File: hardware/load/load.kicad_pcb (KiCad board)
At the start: 2 copper layers, 116 parts, among them J101 vin_kelvin, J102 uart, J103 panel, J105 vin, J106 dut, J107 fan, J108 fuse 20A, J401 temp_sensor, Q302 2sb1357, Q501 2STC4468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

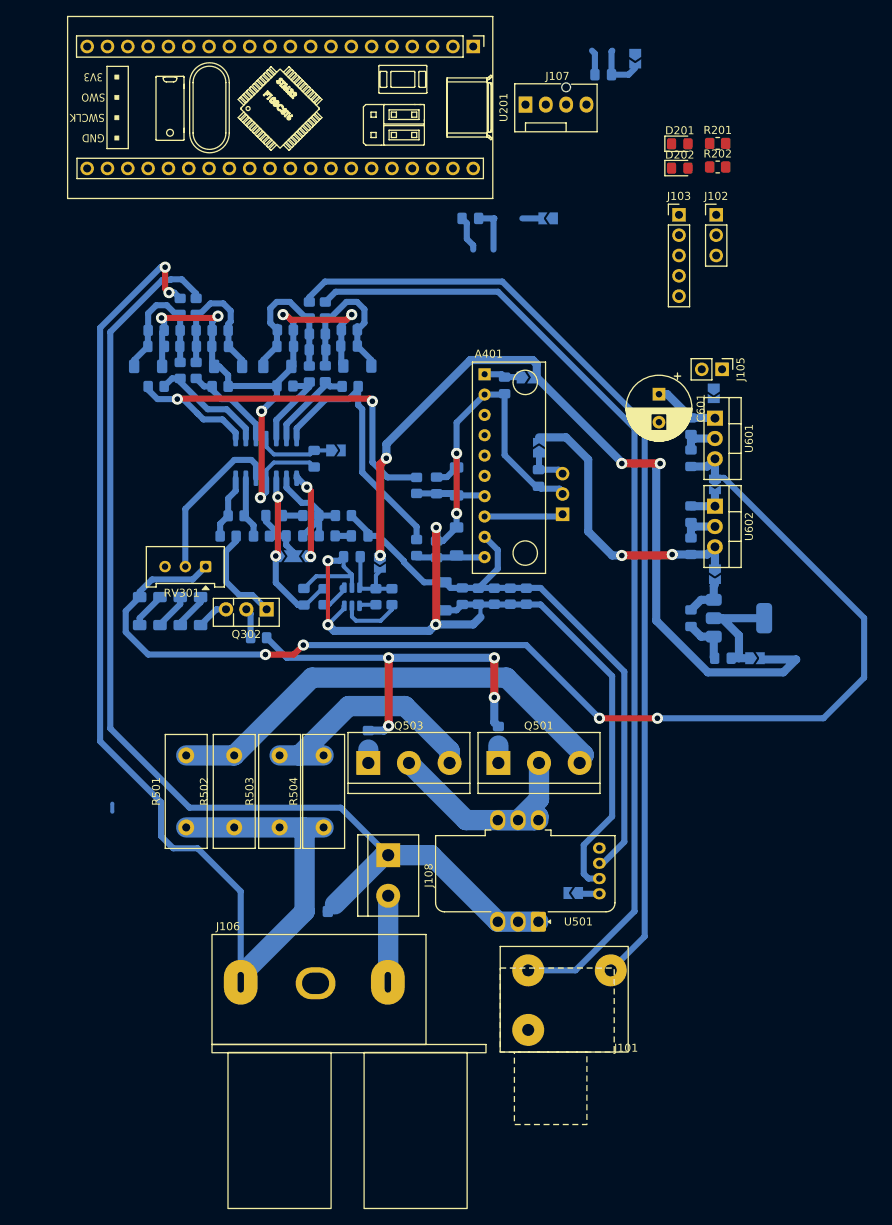
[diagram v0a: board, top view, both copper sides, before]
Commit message: feat(load): route logic and optmize layout
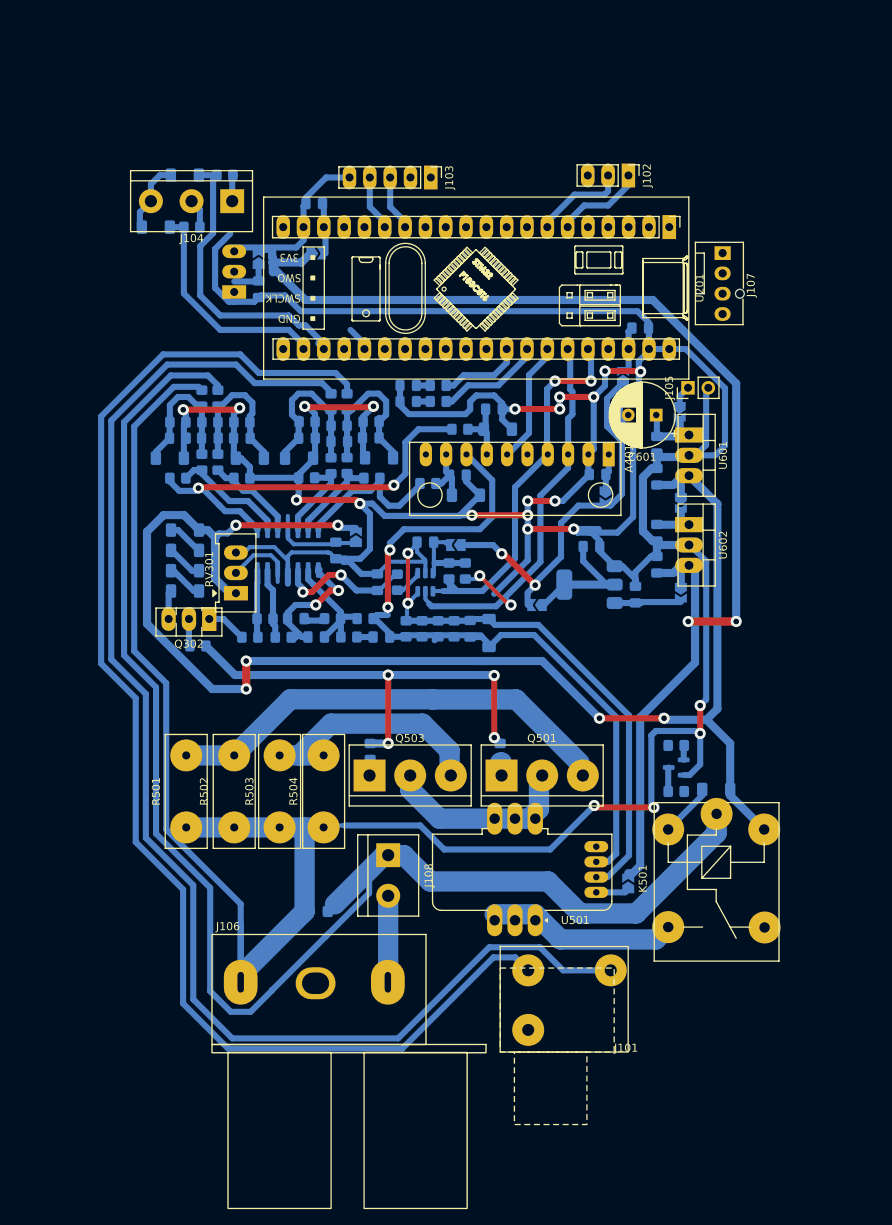
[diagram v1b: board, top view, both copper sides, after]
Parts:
- removed JP301: enable_analog_feedback, Jumper:SolderJumper-3_P2.0mm_Open_TrianglePad1.0x1.5mm
- added D203: 3.3 < V < 5.1, Diode_SMD:D_MiniMELF, B.Cu at (165.0, 56.0)
- added D204: 3.3 < V < 5.1, Diode_SMD:D_MiniMELF, B.Cu at (168.6, 49.5)
- added D501: LL4148, Diode_SMD:D_MiniMELF, B.Cu at (235.0, 126.2)
- added J104: external_trigger, TerminalBlock:TerminalBlock_bornier-3_P5.08mm, F.Cu at (174.5, 52.7)
- added K501: SANYOU_SRD_Form_C, Relay_THT:Relay_SPDT_SANYOU_SRD_Series_Form_C, F.Cu at (235.1, 129.3)
- added Q502: BC817, Package_TO_SOT_SMD:SOT-23, B.Cu at (230.0, 123.5)
- added R203: 2.2k, Resistor_SMD:R_0805_2012Metric_Pad1.20x1.40mm_HandSolder, B.Cu at (173.6, 49.5)
- added R204: 2.2k, Resistor_SMD:R_0805_2012Metric_Pad1.20x1.40mm_HandSolder, B.Cu at (169.5, 56.0)
- added R505: 150R, Resistor_SMD:R_0805_2012Metric_Pad1.20x1.40mm_HandSolder, B.Cu at (230.0, 126.5)
- added R506: 1k, Resistor_SMD:R_0805_2012Metric_Pad1.20x1.40mm_HandSolder, B.Cu at (230.0, 120.8)
- D201, D202, R201, R202: moved to B.Cu
- moved J401 49.6 mm to (174.8, 64.1)
- moved R201 46.2 mm to (200.2, 75.8), turned to 180 degrees
- moved R202 45.6 mm to (200.2, 77.8), turned to 180 degrees
- moved D201 45.4 mm to (196.5, 75.8)
- moved D202 44.8 mm to (196.5, 77.8)
- moved JP404 42.2 mm to (177.8, 60.0)
- moved C414 42.2 mm to (177.8, 63.7)
- moved JP202 39.8 mm to (223.4, 74.7), turned to 90 degrees
- moved U201 33.3 mm to (229.1, 56.0)
- moved C202 32.0 mm to (225.5, 68.6), turned to 0 degrees
- moved J103 31.4 mm to (199.3, 49.8), turned to -90 degrees
- moved J107 30.8 mm to (235.8, 59.2), turned to -90 degrees
- moved JP201 29.3 mm to (185.0, 59.2), turned to 0 degrees
- moved NT501 28.3 mm to (187.8, 130.8), turned to 0 degrees
- moved JP604 28.0 mm to (212.6, 103.2), turned to 180 degrees
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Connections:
- C302 pad 2: Net-(JP301-C) -> Net-(C302-Pad2)
- C303 pad 2: Net-(JP301-C) -> Net-(C302-Pad2)
- R201 pad 1: Net-(U201-PB0) -> Net-(U201-PA7)
- R202 pad 1: Net-(U201-PB1) -> Net-(U201-PB0)
- R304 pad 1: Net-(JP301-C) -> Net-(C302-Pad2)
- U201 pad 13: /analog/alert -> unconnected-(U201-PB5-Pad13)
- U201 pad 22: unconnected-(U201-PC13-Pad22) -> Net-(D203-K)
- U201 pad 23: unconnected-(U201-PC14-Pad23) -> Net-(D204-K)
- U201 pad 31: /stm32/fan -> unconnected-(U201-PA6-Pad31)
- U201 pad 32: unconnected-(U201-PA7-Pad32) -> Net-(U201-PA7)
- U201 pad 34: Net-(U201-PB1) -> /analog/alert
- U201 pad 5: unconnected-(U201-PA8-Pad5) -> /stm32/fan
- U301 pad 8: Net-(JP301-A) -> Net-(C302-Pad2)
- U501 pad 1: /analog/vin+ -> Net-(U501-IN1)
- U501 pad 2: /analog/vin+ -> Net-(U501-IN1)
- U501 pad 3: /analog/vin+ -> Net-(U501-IN1)
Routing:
- net GND: track 210.5 -> 532.5 mm, vias 12 -> 24
- net +5V: track 36.5 -> 157.7 mm
- net +3V3: track 104.2 -> 47.9 mm, vias 4 -> 2
- net /analog/vin_kelvin+: track 120.8 -> 169.7 mm
- net /analog/scl: track 7.74 -> 55.6 mm, vias 0 -> 2
- net /analog/sda: track 1.99 -> 49.3 mm, vias 0 -> 2
- net /analog/vin+: track 138.3 -> 185.2 mm
- net /analog/vin_kelvin-: track 123.0 -> 165.2 mm
- net Net-(D204-K): track 0.00 -> 37.2 mm
- net +12V: track 154.4 -> 186.0 mm, vias 4 -> 6
- net Net-(D203-K): track 0.00 -> 28.5 mm
- net Net-(U501-IN1): track 0.00 -> 23.9 mm
- net Net-(C302-Pad2): track 0.00 -> 18.1 mm, vias 0 -> 2
- net /analog/alert: track 0.00 -> 15.3 mm
- net GNDPWR: track 160.8 -> 146.6 mm, vias 2 -> 0
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
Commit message: feat(load): finzalize power routing and add mounting holes
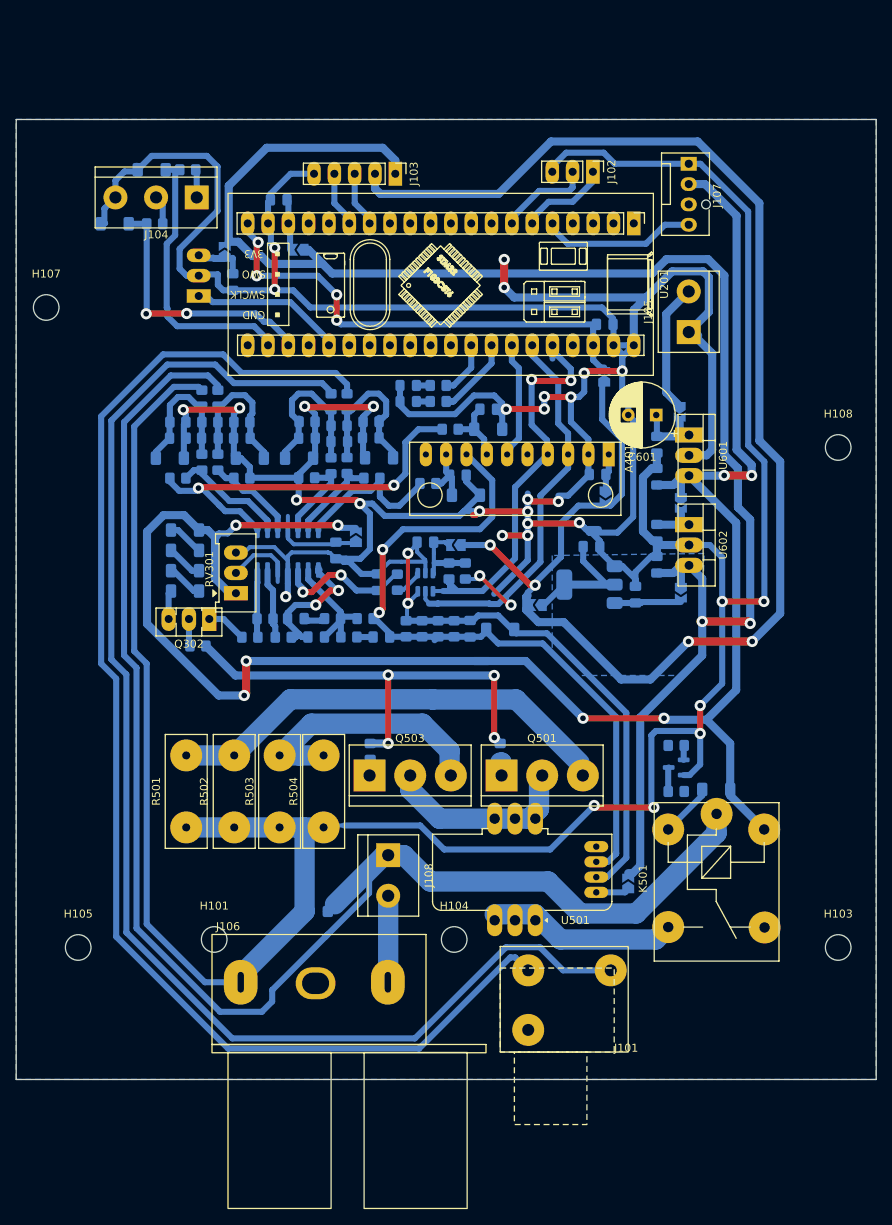
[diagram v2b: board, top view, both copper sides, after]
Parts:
- added H101: MountingHole, MountingHole:MountingHole_3.2mm_M3, F.Cu at (172.2, 145.0)
- added H103: MountingHole, MountingHole:MountingHole_3.2mm_M3, F.Cu at (250.2, 146.0)
- added H104: MountingHole, MountingHole:MountingHole_3.2mm_M3, F.Cu at (202.2, 145.0)
- added H105: MountingHole, MountingHole:MountingHole_3.2mm_M3, F.Cu at (155.2, 146.0)
- added H107: MountingHole, MountingHole:MountingHole_3.2mm_M3, F.Cu at (151.2, 66.0)
- added H108: MountingHole, MountingHole:MountingHole_3.2mm_M3, F.Cu at (250.2, 83.5)
- J105: value vin -> input; footprint Connector_PinHeader_2.54mm:PinHeader_1x02_P2.54mm_Vertical -> TerminalBlock:TerminalBlock_bornier-2_P5.08mm
- moved J107 11.9 mm to (231.6, 48.0)
- moved D204 10.7 mm to (159.8, 55.5)
- moved R203 10.7 mm to (164.8, 55.5)
- moved D203 7.19 mm to (164.4, 48.8)
- moved R204 7.19 mm to (168.9, 48.8)
- moved J105 6.96 mm to (231.6, 69.1)
- moved J401 4.46 mm to (170.3, 64.6)
- moved C201 4.46 mm to (180.3, 52.5)
- moved J102 4.46 mm to (219.6, 49.0)
- moved J104 4.46 mm to (170.1, 52.2)
- moved U201 4.46 mm to (224.7, 55.5)
- moved C202 4.46 mm to (221.1, 68.1)
- moved J103 4.46 mm to (194.9, 49.3)
- moved JP404 4.34 mm to (173.6, 59.0)
- moved C414 3.36 mm to (174.6, 62.8)
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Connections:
- J105 pad 1: /supplies/input -> GND
- J105 pad 2: GND -> /supplies/input
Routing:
- net +3V3: track 47.9 -> 196.5 mm, vias 2 -> 4
- net GND: track 532.5 -> 672.6 mm, vias 24 -> 33
- net /stm32/enable_3v3_stm: track 5.72 -> 61.0 mm, vias 0 -> 4
- net +12V: track 186.0 -> 237.7 mm, vias 6 -> 8
- net +5V: track 157.7 -> 200.9 mm
- net /stm32/fan: track 0.00 -> 19.4 mm
- net /analog/temperature_adc: track 3.11 -> 19.2 mm
- net /supplies/input: track 2.71 -> 16.2 mm
- net Net-(D203-K): track 28.5 -> 35.0 mm
- net GNDPWR: track 146.6 -> 141.9 mm
- net Net-(D204-K): track 37.2 -> 32.8 mm, vias 0 -> 2
- net Net-(U201-PA7): track 10.5 -> 6.85 mm
- net /analog/sda: track 49.3 -> 52.8 mm
- net /analog/5_temp_sensor: track 5.07 -> 7.91 mm
- net Net-(U201-PB0): track 13.4 -> 10.6 mm
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- added copper zone on B.Cu, net GND
- added copper zone on B.Cu, net Net-(JP604-A)
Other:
- board outline added: 107.5 x 120 mm

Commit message: feat(load): fix DRC errors and warinigs
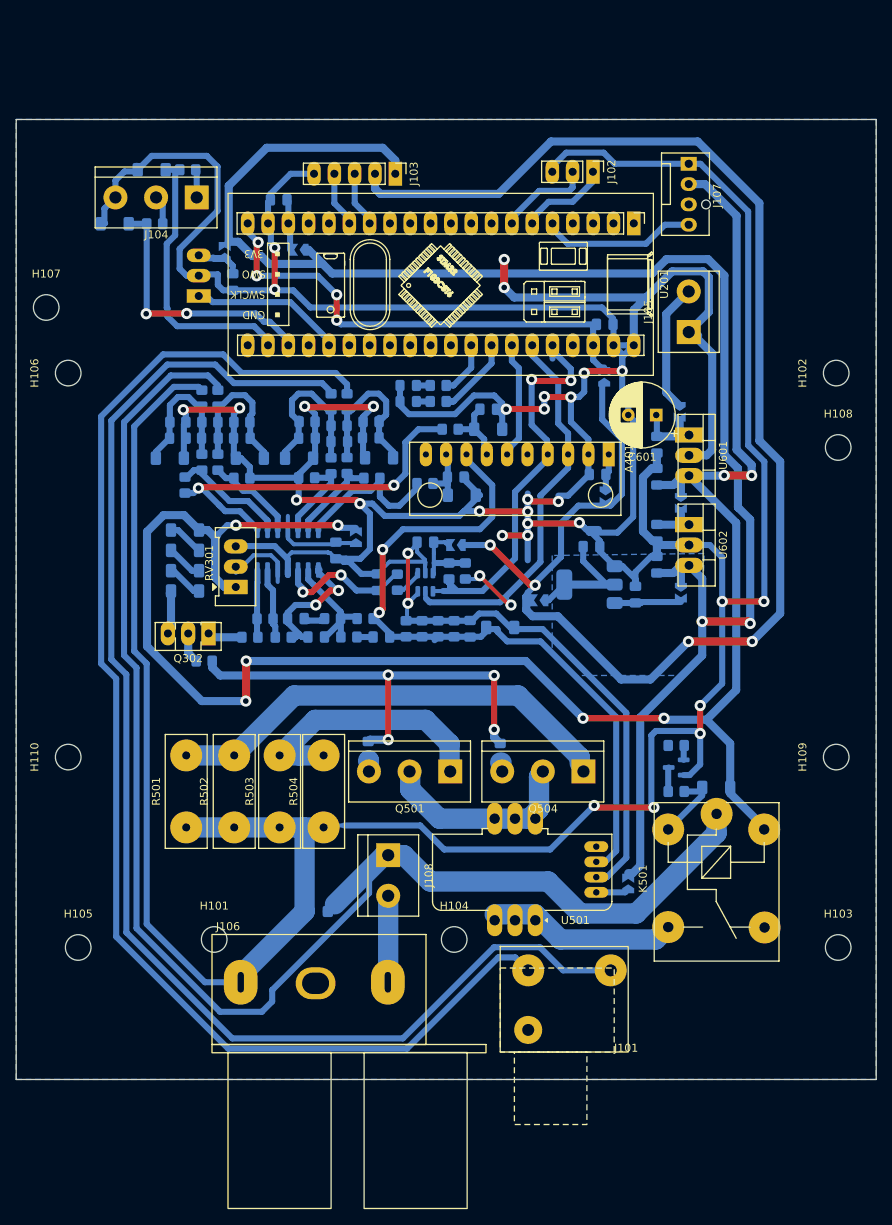
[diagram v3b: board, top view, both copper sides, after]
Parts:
- removed Q503: 2STC4468, TerminalBlock:TerminalBlock_bornier-3_P5.08mm
- added H102: MountingHole, MountingHole:MountingHole_3.2mm_M3, F.Cu at (250.0, 74.2)
- added H106: MountingHole, MountingHole:MountingHole_3.2mm_M3, F.Cu at (154.0, 74.2)
- added H109: MountingHole, MountingHole:MountingHole_3.2mm_M3, F.Cu at (250.0, 122.2)
- added H110: MountingHole, MountingHole:MountingHole_3.2mm_M3, F.Cu at (154.0, 122.2)
- added Q504: 2STC4468, TerminalBlock:TerminalBlock_bornier-3_P5.08mm, F.Cu at (218.4, 124.0)
- JP201, JP202, JP401, JP402, JP403, JP404, JP501, JP601, JP602, JP603, JP604: footprint Jumper:SolderJumper-2_P1.3mm_Open_TrianglePad1.0x1.5mm -> Load:SolderJumper-2_P1.3mm_Open_TrianglePad1.0x1.5mm
- moved Q501 6.44 mm to (201.8, 124.0), turned to 180 degrees
- moved R307 2.04 mm to (171.0, 110.2)
- moved Q302 1.81 mm to (171.5, 106.8)
- moved R421 1.24 mm to (168.6, 88.2), turned to -90 degrees
- moved RV301 0.78 mm to (174.9, 100.9)
- moved JP604 0.62 mm to (212.8, 102.6)
- moved D407 0.52 mm to (203.2, 89.5)
- moved R424 0.37 mm to (198.6, 88.0)
- moved C409 0.36 mm to (202.4, 87.2)
- moved R102 0.35 mm to (191.5, 121.2)
- moved D405 0.25 mm to (208.0, 106.0)
- moved D501 0.25 mm to (235.0, 126.0)
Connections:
- Q501 pad 1: /power/base1 -> Net-(Q501-E)
- Q501 pad 3: Net-(Q501-E) -> /power/base2
- R501 pad 2: Net-(Q501-E) -> Net-(Q504-E)
- R502 pad 2: Net-(Q501-E) -> Net-(Q504-E)
- R503 pad 2: Net-(Q503-E) -> Net-(Q501-E)
- R504 pad 2: Net-(Q503-E) -> Net-(Q501-E)
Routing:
- net Net-(Q504-E): track 0.00 -> 56.2 mm
- net Net-(Q503-E): track 31.3 -> 0.00 mm
- net Net-(Q501-E): track 55.4 -> 32.2 mm
- net GND: track 672.6 -> 663.1 mm, vias 33 -> 32
- net /power/base2: track 0.00 -> 2.75 mm
- net Net-(D501-A): track 6.76 -> 9.47 mm
- net Net-(R421-Pad2): track 50.1 -> 47.4 mm
- net Net-(D304-K): track 3.76 -> 5.89 mm
- net /power/base1: track 1.79 -> 0.17 mm
- net /driver/transistor_base: track 57.3 -> 56.0 mm
- net Net-(Q302-B): track 5.02 -> 4.36 mm
- net Net-(Q302-C): track 4.58 -> 3.93 mm
- net +12V: track 237.7 -> 238.3 mm
- net /analog/vin_kelvin_out: track 7.53 -> 7.03 mm
